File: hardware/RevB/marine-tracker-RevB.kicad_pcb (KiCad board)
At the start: 4 copper layers, 65 x 58 mm, 108 parts, among them J1 USB-C, J2 BATTERY, J3 LTE_U.FL, J4 GNSS_L1_L5_U.FL, J5 Nano_SIM, Q1 AO3401A_REVERSE_POLARITY, Q2 MMBT2222A, U1 A7670G-LABE, U10 TPS3808G09DBVR, U11 TPL5111DDCR, U12 SN74LVC2G08DCUR, U13 SN74LVC1G14DBVR, U2 LC29H-AA, U3 BQ24074RGTR, U4 TPS7A2033PDBV, U5 TXS0104EPW, U6 W25Q32JWSSIM, U7 TPS22917DBV_GNSS_LOAD, U8 TPL5010_10MIN_WATCHDOG, U9 TPS3839K33DBZR

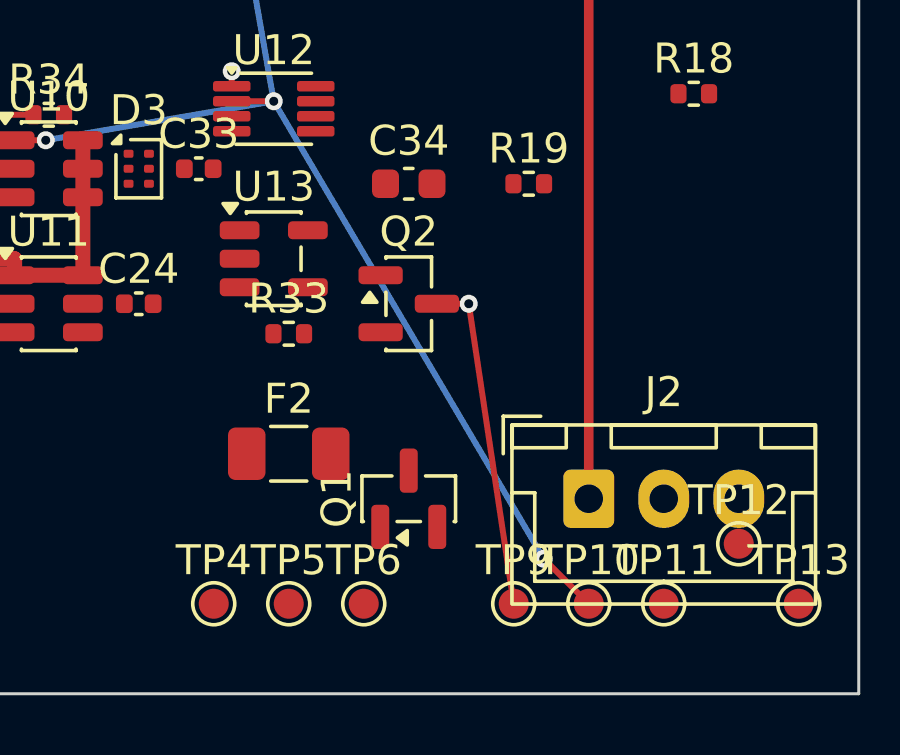
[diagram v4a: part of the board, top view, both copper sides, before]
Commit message: checkpoint: establish RevB power routing authority and close BAT gate
Documents the project owner's Power/Charger routing authority (PromptID 103):
POWER_HIGH (1.00mm, battery path), POWER_MEDIUM (0.50mm, USB VBUS),
ANALOG_SENSE and LOGIC_CONTROL (0.25mm) classes, derived from F1/F2 fuse
ratings and cross-checked against existing VSYS/VBAT_MODEM precedents.
PWR_FLAG routing withheld pending schematic clarification; VDD_1V8 excluded
pending a separate source/load audit.

Routes BAT_GATE (Q1 battery-FET gate control, PromptID 104): F.Cu escapes
with an In2.Cu dogleg trunk routed around PWRKEY's via, avoiding the dense
Q1/Q2/F2/U13/C34 footprint cluster where direct/local F.Cu attempts all
collided. Native rule-area-aware preflight passed for every segment and via
before write; post-write DRC shows zero new route-attributable violations.
The high-current battery corridor (BAT_PACK_POS/BAT_PROTECTED/BAT_CELL,
still unrouted) was not consumed by this route.
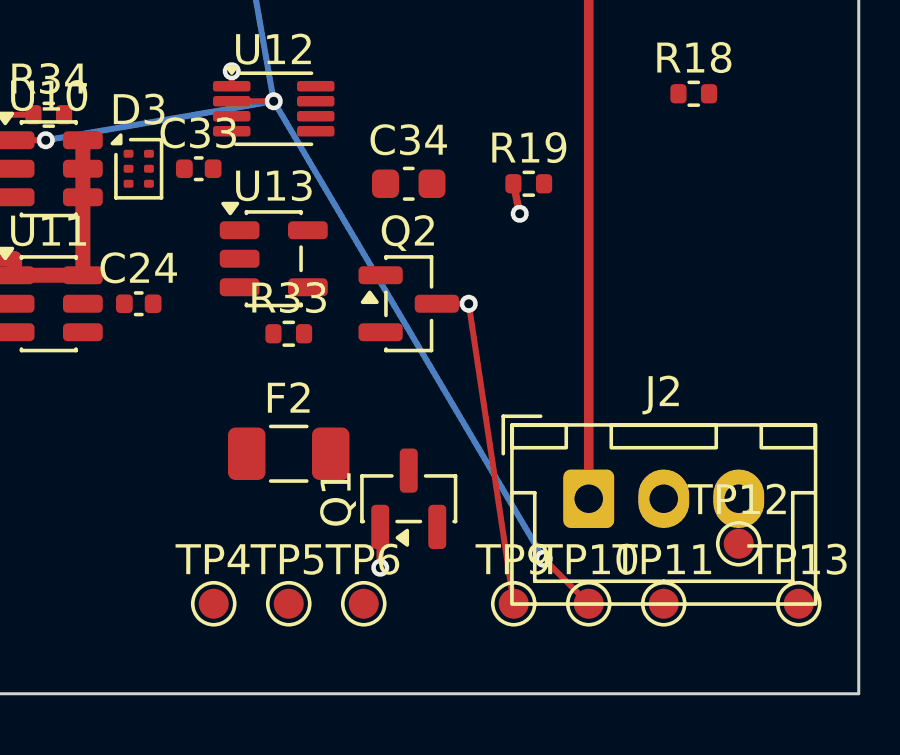
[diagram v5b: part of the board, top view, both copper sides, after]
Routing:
- net BAT_GATE: track 0.00 -> 16.4 mm, vias 0 -> 2
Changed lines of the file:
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@@
+	)
+	(segment
+		(start 53.7 42)
+		(end 53.49 41)
+		(width 0.25)
+		(layer "F.Cu")
+		(net "BAT_GATE")
+	)
+	(segment
+		(start 49.05 52.4375)
+		(end 49.05 53.8)
+		(width 0.25)
+		(layer "F.Cu")
+		(net "BAT_GATE")
+	)
+	(via
+		(at 49.05 53.8)
+		(size 0.6)
+		(drill 0.3)
+		(layers "F.Cu" "B.Cu")
+		(net "BAT_GATE")
+	)
+	(via
+		(at 53.7 42)
+		(size 0.6)
+		(drill 0.3)
+		(layers "F.Cu" "B.Cu")
+		(net "BAT_GATE")
+	)
+	(segment
+		(start 55 46)
+		(end 53.7 42)
+		(width 0.25)
+		(layer "In2.Cu")
+		(net "BAT_GATE")
+	)
+	(segment
+		(start 49.05 53.8)
+		(end 55 46)
+		(width 0.25)
+		(layer "In2.Cu")
+		(net "BAT_GATE")
 	)
 	(segment
